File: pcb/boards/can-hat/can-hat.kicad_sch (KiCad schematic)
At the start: 26 parts, among them J1 Raspberry_Pi_GPIO, J2 OBD-II, J3 CAN_Term, J4 Audio, U1 AMS1117-3.3, U2 MCP2515, U3 SN65HVD230, Y1 16MHz

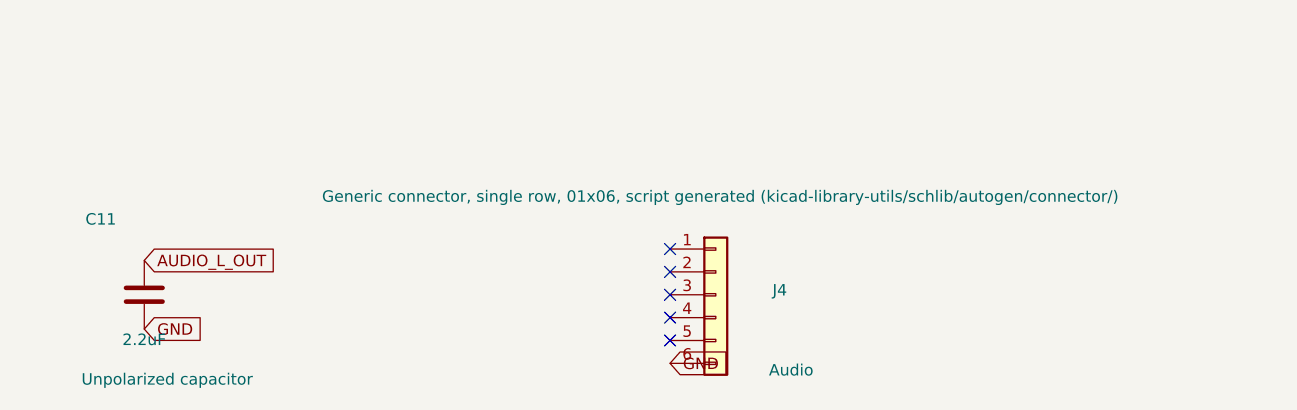
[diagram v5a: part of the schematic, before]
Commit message: CAN HAT PCB: Complete routing via FreeRouting with ground pour
- SMD components (caps, resistors, ferrites) moved to back layer
- GPIO header J1 pads flipped to correct pin orientation
- Auto-routed via FreeRouting, manual fix for CANL trace
- B.Cu ground pour with thermal reliefs
- DRC: 61 warnings (all cosmetic - mounting holes, text orientation)
- 0 unconnected pads, board ready for manufacturing

Co-Authored-By: Claude Opus 4.5 <noreply@anthropic.com>
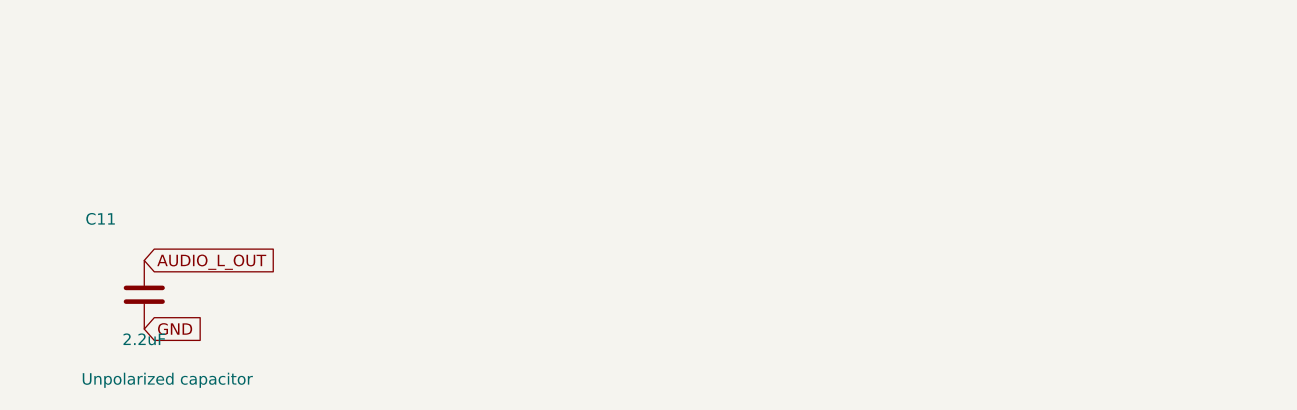
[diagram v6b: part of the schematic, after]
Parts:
- removed J4: Audio, Connector_PinHeader_2.54mm:PinHeader_1x06_P2.54mm_Vertical, symbol Connector_Generic:Conn_01x06
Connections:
- no-connect marks 47 -> 42
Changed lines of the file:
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@@
 	)
 	(no_connect
-		(at 820.42 756.92)
-	)
-	(no_connect
-		(at 820.42 759.46)
-	)
-	(no_connect
-		(at 820.42 762)
-	)
-	(no_connect
-		(at 820.42 764.54)
-	)
-	(no_connect
-		(at 820.42 767.08)
-	)
-	(no_connect
 		(at 207.62 144.92)
 	)
@@
 		)
 	)
-	(global_label "GND"
-		(shape input)
-		(at 820.42 769.62 0)
-		(fields_autoplaced yes)
-		(effects
-			(font
-				(size 1.27 1.27)
-			)
-			(justify left)
-		)
-		(property "Intersheetrefs" "${INTERSHEET_REFS}"
-			(at 820.42 769.62 0)
-			(effects
-				(font
-					(size 1.27 1.27)
-				)
-				(hide yes)
-			)
-		)
-	)
 	(global_label "+3.3V"
 		(shape input)
@@
 					(unit 1)
 				)
-			)
-		)
-	)
-	(symbol
-		(lib_id "Connector_Generic:Conn_01x06")
-		(at 825.5 762 0)
-		(unit 1)
-		(exclude_from_sim no)
-		(in_bom yes)
-		(on_board yes)
-		(dnp no)
-		(property "Reference" "J4"
-			(at 832.612 761.492 0)
-			(effects
-				(font
-					(size 1.27 1.27)
-				)
-			)
-		)
-		(property "Value" "Audio"
-			(at 833.882 770.382 0)
-			(effects
-				(font
-					(size 1.27 1.27)
-				)
-			)
-		)
-		(property "Footprint" "Connector_PinHeader_2.54mm:PinHeader_1x06_P2.54mm_Vertical"
-			(at 825.5 762 0)
-			(effects
-				(font
-					(size 1.27 1.27)
-				)
-				(hide yes)
-			)
-		)
-		(property "Datasheet" "~"
-			(at 825.5 762 0)
-			(effects
-				(font
-					(size 1.27 1.27)
-				)
-				(hide yes)
-			)
-		)
-		(property "Description" "Generic connector, single row, 01x06, script generated (kicad-library-utils/schlib/autogen/connector/)"
-			(at 826.008 751.078 0)
-			(effects
-				(font
-					(size 1.27 1.27)
-				)
-			)
-		)
-		(pin "3"
-		)
-		(pin "2"
-		)
-		(pin "4"
-		)
-		(pin "1"
-		)
-		(pin "5"
-		)
-		(pin "6"
-		)
-		(instances
-			(project "can-hat"
-				(path "/7bb601d0-af23-47b8-978e-986fbee2569f"
-					(reference "J4")
-					(unit 1)
-				)
-			)
-			(project "wrx-power-can-hat-AUTO"
-				(path "/95587948-5deb-4ec6-b123-ccc764cd888f"
-					(reference "J7")
-					(unit 1)
-				)
